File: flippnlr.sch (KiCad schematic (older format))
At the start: 90 parts, among them J1 Data In, J2 Data Out, J8 12V, U1 SN74HCS594, U10 TPL7407LA, U11 TPL7407LA, U12 SN74HCS365, U13 LD1117 3.3V, U2 SN74HCS594, U3 SN74HCS594, U4 SN74HCS594, U5 SN74HCS594, U6 TPL7407LA, U7 TPL7407LA, U8 TPL7407LA, U9 TPL7407LA

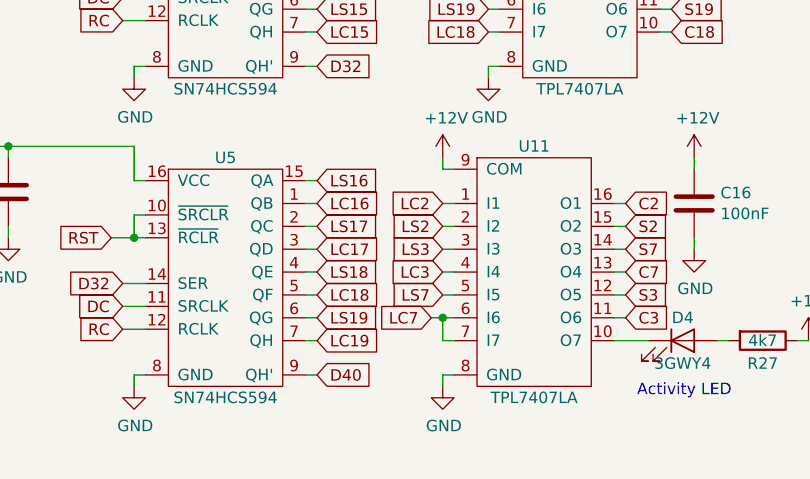
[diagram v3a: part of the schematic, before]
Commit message: correct Lx3/Lx7
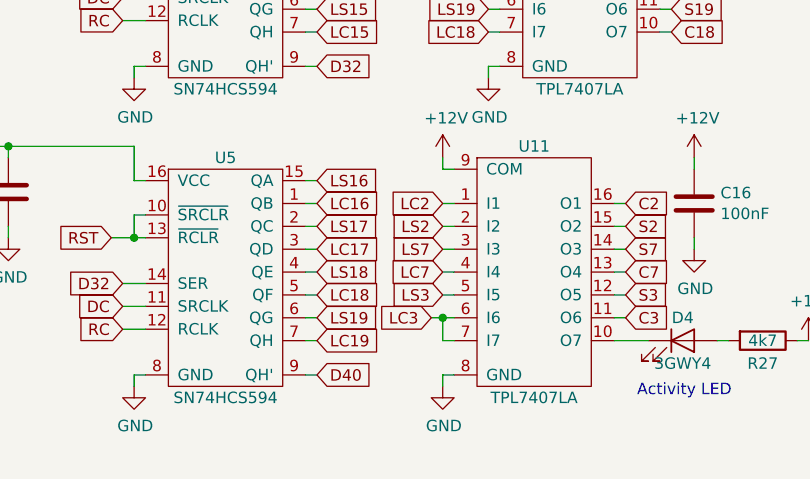
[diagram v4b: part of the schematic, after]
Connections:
- net LC3: now also U11.6 (I6), U11.7 (I7); no longer U11.4 (I4)
- net LC7: now also U11.4 (I4); no longer U11.6 (I6), U11.7 (I7)
- net LS3: now also U11.5 (I5); no longer U11.3 (I3)
- net LS7: now also U11.3 (I3); no longer U11.5 (I5)
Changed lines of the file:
@@
 Text GLabel 4950 6600 0    50   Input ~ 0
 LS2
+Text GLabel 4950 6900 0    50   Input ~ 0
+LS3
+Text GLabel 4900 7000 0    50   Input ~ 0
+LC3
 Text GLabel 4950 6700 0    50   Input ~ 0
-LS3
+LS7
 Text GLabel 4950 6800 0    50   Input ~ 0
-LC3
-Text GLabel 4950 6900 0    50   Input ~ 0
-LS7
-Text GLabel 4900 7000 0    50   Input ~ 0
 LC7
 Wire Wire Line

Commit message: first prototype
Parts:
- R21: value 1k -> 4k7
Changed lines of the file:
@@
 U 1 1 6131F7AE
 P 3400 1050
-F 0 "R21" H 3250 1100 50  0000 L CNN
-F 1 "1k" H 3250 1000 50  0000 L CNN
+F 0 "R21" H 3200 1100 50  0000 L CNN
+F 1 "4k7" H 3200 1000 50  0000 L CNN
 F 2 "Resistor_SMD:R_0805_2012Metric_Pad1.15x1.40mm_HandSolder" V 3330 1050 50  0001 C CNN
 F 3 "~" H 3400 1050 50  0001 C CNN
